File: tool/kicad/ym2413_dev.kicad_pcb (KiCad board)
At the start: 2 copper layers, 0.8 x 5.6 mm, 147 parts, among them IC1 6N135, J1 MICRO-USB-AB, K1 CONN_3, K2 CONN_3, P1 TEST_POINT, P10 TEST_POINT, P11 TEST_POINT, P12 TEST_POINT, P13 TEST_POINT, P14 TEST_POINT, P15 TEST_POINT, P16 TEST_POINT, P17 TEST_POINT, P18 TEST_POINT, P19 TEST_POINT, P2 TEST_POINT, P20 TEST_POINT, P21 TEST_POINT, P22 TEST_POINT, P23 TEST_POINT, P24 TEST_POINT, P25 TEST_POINT, P26 TEST_POINT, P27 TEST_POINT, P28 TEST_POINT, P29 TEST_POINT, P3 TEST_POINT, P30 CONN_3X2, P31 CONN_2, P32 CONN_2, P33 TEST_POINT, P34 TEST_POINT, P35 CONN_6, P36 CONN_5, P37 TEST_POINT, P38 TEST_POINT, P4 TEST_POINT, P5 MIDI-IN, P6 TEST_POINT, P7 TEST_POINT, P8 TEST_POINT, P9 TEST_POINT, U1 SN74LVC2T45, U2 ST-USBLC6-2, U3 EFM32GG332, U4 YM2413, U5 LM386, U6 LM386, X1 48Mhz, X2 CRYSTAL

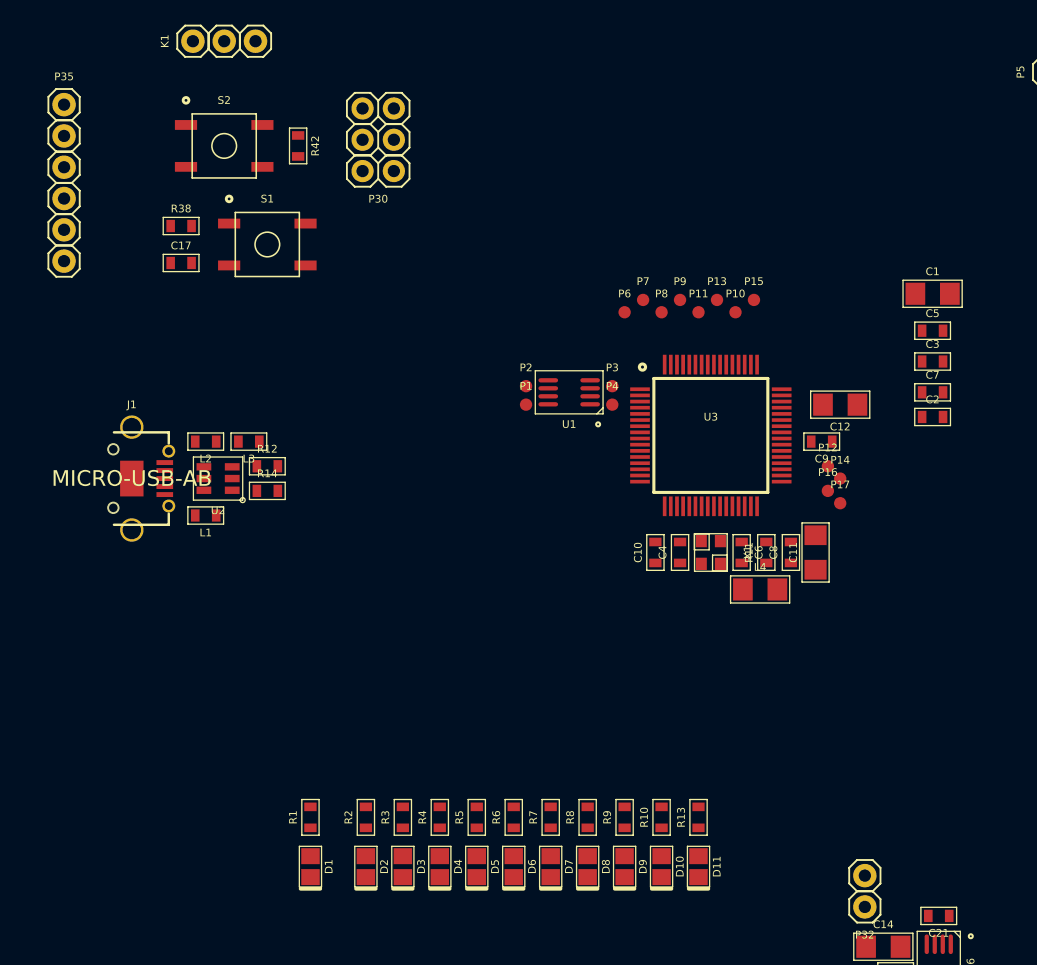
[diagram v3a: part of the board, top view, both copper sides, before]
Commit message: slightly tighen layout
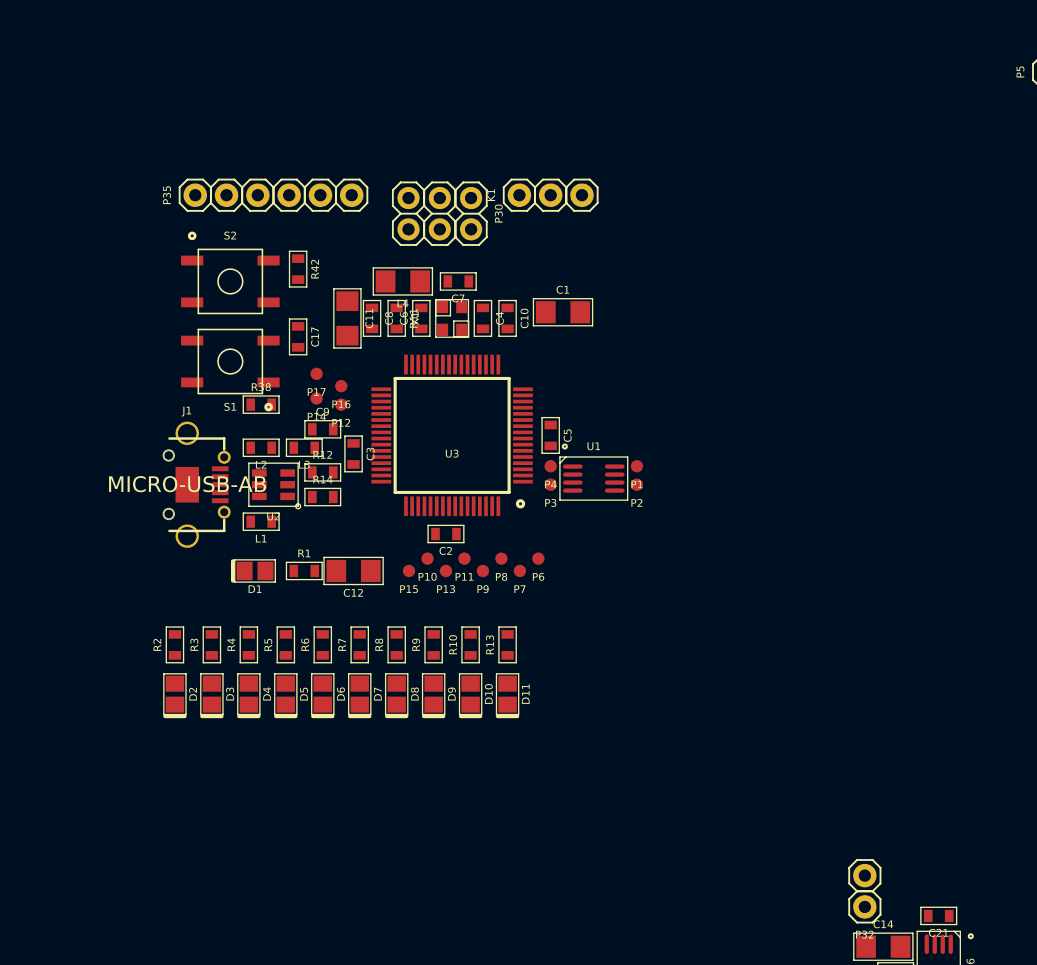
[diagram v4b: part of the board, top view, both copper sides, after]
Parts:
- moved C3 47.6 mm to (58.0, 83.0), turned to 270 degrees
- moved P17 43.8 mm to (55.0, 76.5), turned to 180 degrees
- moved P14 43.0 mm to (55.0, 78.5), turned to 180 degrees
- moved C11 42.5 mm to (57.5, 72.0), turned to 270 degrees
- moved C12 41.7 mm to (58.0, 92.5)
- moved C2 40.6 mm to (65.5, 89.5), turned to 180 degrees
- moved C9 40.5 mm to (55.5, 81.0), turned to 0 degrees
- moved P16 40.4 mm to (57.0, 77.5), turned to 180 degrees
- moved P12 39.8 mm to (57.0, 79.0), turned to 180 degrees
- moved C7 39.5 mm to (66.5, 69.0), turned to 180 degrees
- moved C8 38.9 mm to (59.5, 72.0), turned to 270 degrees
- moved L4 38.3 mm to (62.0, 69.0), turned to 180 degrees
- moved P15 35.6 mm to (62.5, 92.5), turned to 180 degrees
- moved R11 35.5 mm to (61.5, 72.0), turned to 270 degrees
- moved C6 32.2 mm to (63.5, 72.0), turned to 90 degrees
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
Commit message: fix used optocoupler
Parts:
- removed IC1: 6N135, DIL8
- removed P36: CONN_5, PIN_1X5_S
- removed R16: 220, 0603_S
- added U7: ACPL-M21L, SO-5, F.Cu at (107.0, 66.0)
- moved R15 29.3 mm to (104.0, 62.0), turned to 90 degrees
- moved D12 21.7 mm to (100.0, 66.0), turned to 270 degrees
- moved P5 11.0 mm to (112.5, 60.5)

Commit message: fix audio footprint; add to board
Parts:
- K2: footprint PIN_1X3 -> SPC-FD05-3.5mm-stereo-phone-jack
- P5: footprint PIN_1X5_S -> spiratronics-DIN5-midi
- moved P5 10.3 mm to (122.7, 59.0), turned to 270 degrees
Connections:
- K2 pad 1: /ROA3 -> GND
- K2 pad 3: GND -> /ROA3

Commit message: rough layout
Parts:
- moved K2 57.9 mm to (151.0, 95.0), turned to 180 degrees
- moved R52 54.3 mm to (139.0, 90.5), turned to 180 degrees
- moved R54 52.2 mm to (140.0, 93.5), turned to 270 degrees
- moved R49 49.0 mm to (137.5, 93.5), turned to 90 degrees
- moved C23 46.9 mm to (135.0, 92.5), turned to 90 degrees
- moved R37 45.3 mm to (129.5, 89.0)
- moved C14 39.9 mm to (125.5, 91.5), turned to 90 degrees
- moved U6 39.6 mm to (129.5, 93.0)
- moved C21 38.2 mm to (132.5, 93.5), turned to 270 degrees
- moved C15 37.7 mm to (79.5, 93.0)
- moved C16 37.7 mm to (79.5, 98.0)
- moved C18 37.7 mm to (115.0, 83.5)
- moved C19 37.7 mm to (115.0, 80.0)
- moved JP1 37.7 mm to (91.0, 100.5)
- moved JP2 37.7 mm to (98.5, 98.5)
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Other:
- board size 0.8 x 5.6 mm -> 115 x 45 mm
- net class Default: clearance 0.254 -> 2.032
- rule trace_clearance: 0.254 -> 2.032

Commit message: ERC fixes
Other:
- net class Default: clearance 2.032 -> 0.1524
- rule trace_clearance: 2.032 -> 0.1524
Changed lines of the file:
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@@
   (setup
     (last_trace_width 0.254)
-    (trace_clearance 2.032)
+    (trace_clearance 0.1524)
     (zone_clearance 0.508)
     (zone_45_only no)
@@
   (net 126 N-0000098)
   (net_class Default "This is the default net class."
-    (clearance 2.032)
+    (clearance 0.1524)
     (trace_width 0.254)
     (via_dia 0.889)
